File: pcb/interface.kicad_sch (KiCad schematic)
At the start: 9 parts

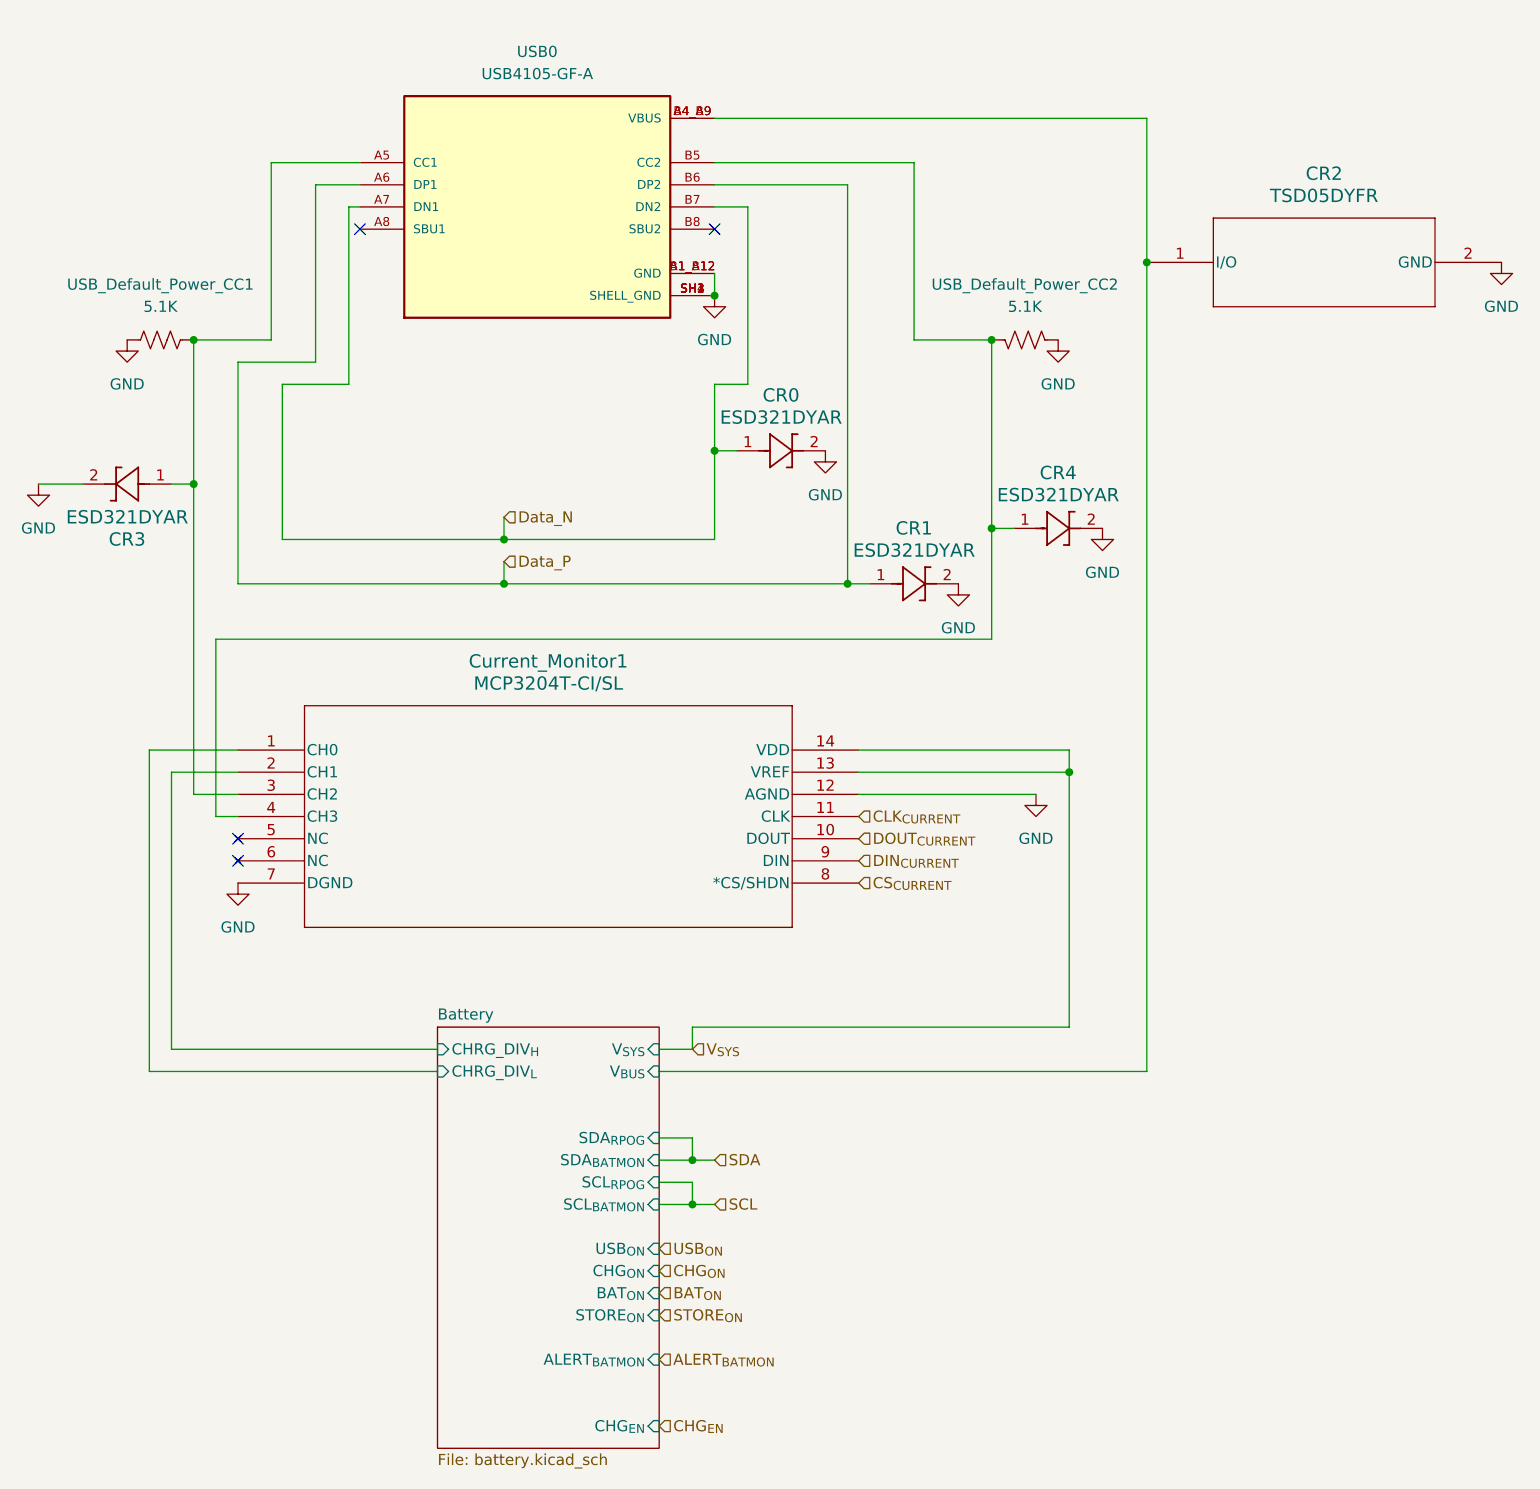
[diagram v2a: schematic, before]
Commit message: Relabel right hand
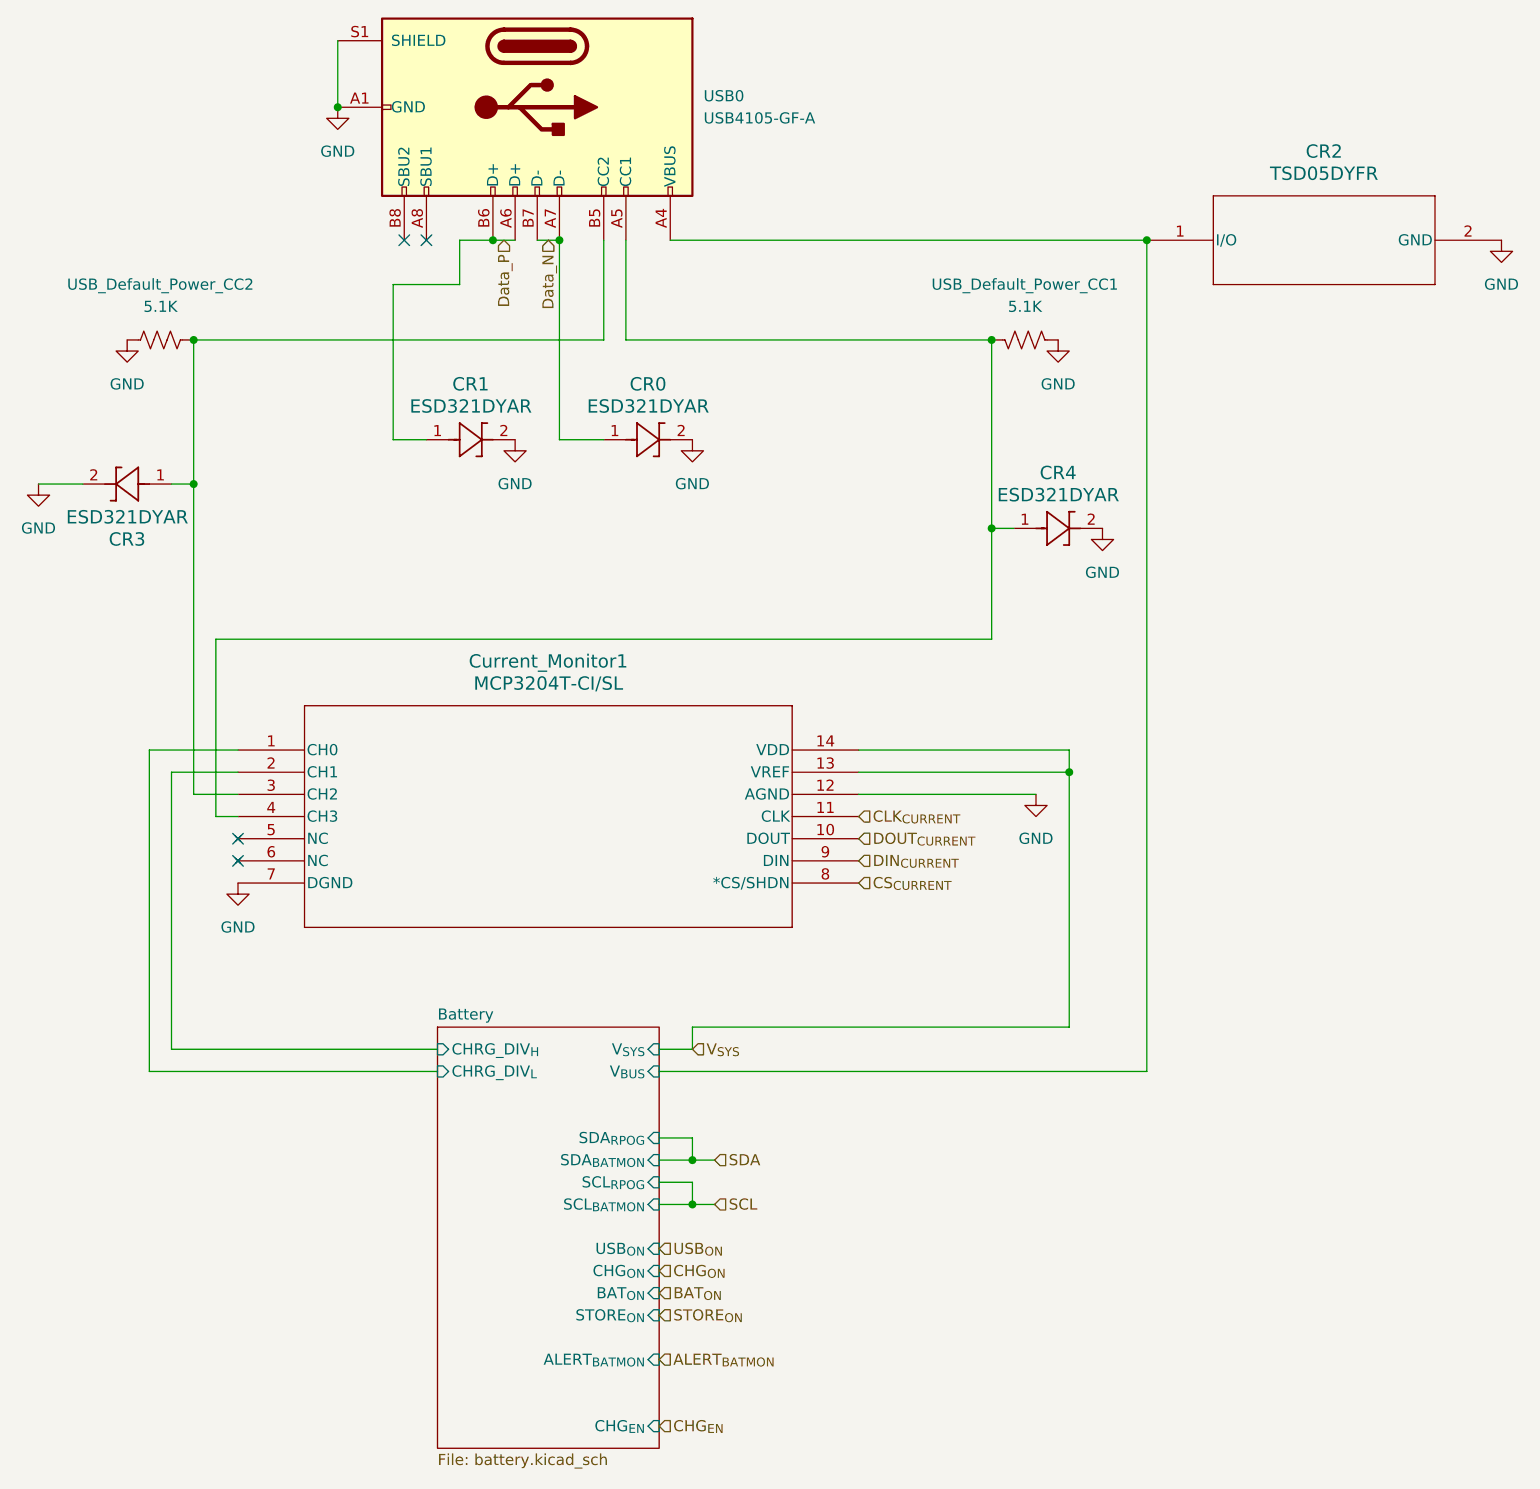
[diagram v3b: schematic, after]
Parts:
- USB0: footprint USB4105-GF-A:GCT_USB4105-GF-A -> USB_C_Receptacle_GCT_USB4105-xx-A_16P_TopMnt_Horizontal; symbol USB4105-GF-A:USB4105-GF-A -> Connector:USB_C_Receptacle_USB2.0_16P
- renumbered USB_Default_Power_CC2 to USB_Default_Power_CC1, USB_Default_Power_CC1 to USB_Default_Power_CC2
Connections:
- net Battery/V_{BUS}: now also USB0.A4 (VBUS), USB0.A9 (VBUS), USB0.B4 (VBUS), USB0.B9 (VBUS); no longer USB0.A4_B9 (VBUS), USB0.B4_A9 (VBUS)
- net GND: now also USB0.A1 (GND), USB0.A12 (GND), USB0.B1 (GND), USB0.B12 (GND), USB0.S1 (SHIELD); no longer USB0.A1_B12 (GND), USB0.B1_A12 (GND), USB0.SH1 (SHELL_GND), USB0.SH2 (SHELL_GND), USB0.SH3 (SHELL_GND), USB0.SH4 (SHELL_GND)
- net at CR3.1, Current_Monitor1.3 (CH2), USB_Default_Power_CC2.1: now also USB0.B5 (CC2); no longer USB0.A5 (CC1)
- net at CR4.1, Current_Monitor1.4 (CH3), USB_Default_Power_CC1.1: now also USB0.A5 (CC1); no longer USB0.B5 (CC2)
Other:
- moved on the sheet: CR0, CR1, CR2

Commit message: Label LCSC
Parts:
- USB_Default_Power_CC1, USB_Default_Power_CC2: LCSC (none) -> C27834
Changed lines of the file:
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@@
 	(title_block
 		(title "Stenoswitch")
-		(date "2025-11-10")
+		(date "2025-11-16")
 		(rev "0.4")
 		(company "https://github.com/Bennett-Petzold/port_plover")
@@
 			)
 		)
+		(property "LCSC" "C27834"
+			(at 102.87 57.15 90)
+			(effects
+				(font
+					(size 1.27 1.27)
+				)
+				(hide yes)
+			)
+		)
 		(pin "2"
 		)
@@
 			(effects
 				(font
+					(size 1.27 1.27)
+				)
+				(hide yes)
+			)
+		)
+		(property "LCSC" "C27834"
+			(at 201.93 57.15 90)
+			(effects
+				(font
